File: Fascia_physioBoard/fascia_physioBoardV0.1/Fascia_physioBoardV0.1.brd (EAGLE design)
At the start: 37.3 x 39.1 mm, 88 parts, among them CN2 CA0612KRX7R9BB102, CN3 CA0612KRX7R9BB102, CN4 CA0612KRX7R9BB102, CN5 CA0612KRX7R9BB102, CN6 CA0612KRX7R9BB102, J1 MOLEX_52437-2471MOLEX_52437-2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, J2 MOLEX_52437-2471MOLEX_52437-2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, J3 MOLEX_51296-1294MOLEX_51296-1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, U1 ADS1299-X, U10 TPD4E1B06DCKR, U11 TPD4E1B06DCKR, U12 OPA320AIDBVRDBV5-L, U13 ADUM5028, U2 OPA2320AIDGKT_NOVA8-SOIC-L, U3 OPA2320AIDGKT_NOVAL8-SOIC-L, U4 HCNR200-300E, U5 OPA320AIDBVRDBV5-L, U6 TPD4E1B06DCKR, U7 TPD4E1B06DCKR, U8 TPD4E1B06DCKR, U9 TPD4E1B06DCKR

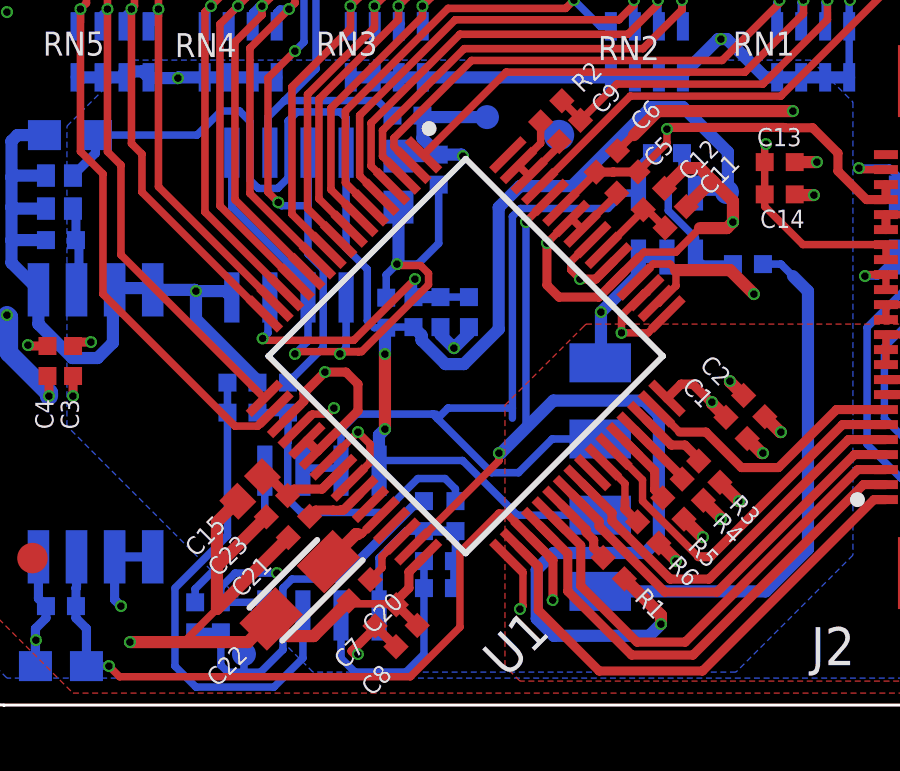
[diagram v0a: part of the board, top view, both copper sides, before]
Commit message: changes to issue with R13
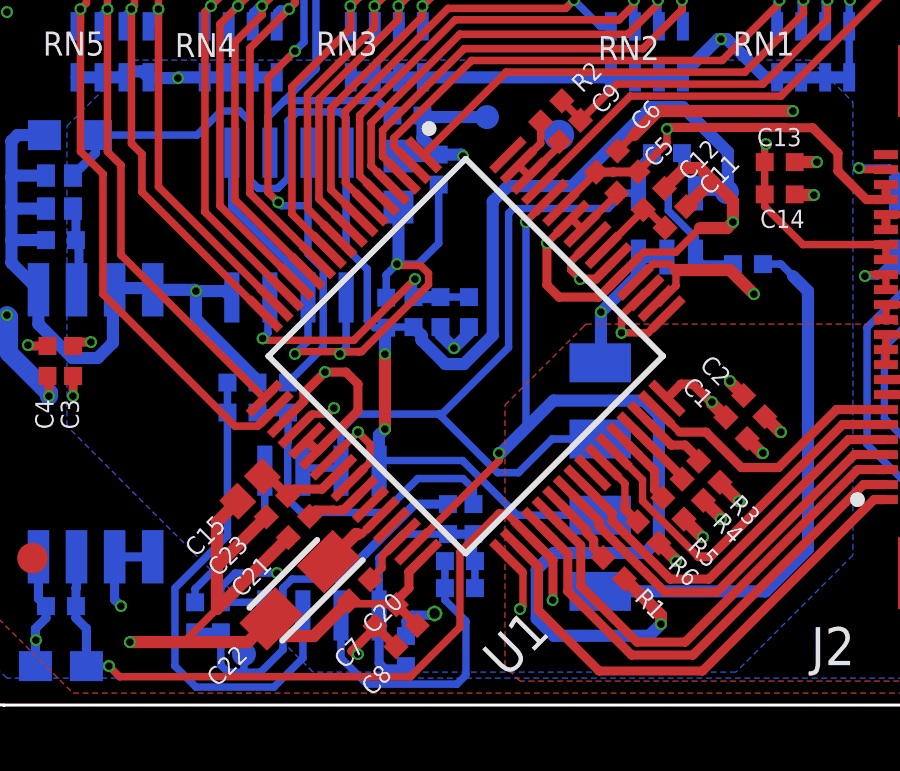
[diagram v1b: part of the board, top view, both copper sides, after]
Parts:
- added R13: 10K, novaXR:0402-TIGHT
- moved R14 0.81 mm to (18.5, 7.40)
- moved C29 0.70 mm to (18.9, 6.00)
- moved R12 0.70 mm to (18.9, 5.10)
- moved C30 0.61 mm to (19.4, 7.40)
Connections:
- net GND_ISO: now also R13.2
- net N$11: now also R13.1
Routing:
- net N$11: track 6.75 -> 9.87 mm
- net N$10: track 7.73 -> 10.2 mm
- net N$15: track 28.3 -> 26.6 mm
- net GND_ISO: track 41.3 -> 42.8 mm, vias 5 -> 6
- net N$4: track 13.0 -> 13.8 mm
- net N$1: track 10.7 -> 11.4 mm

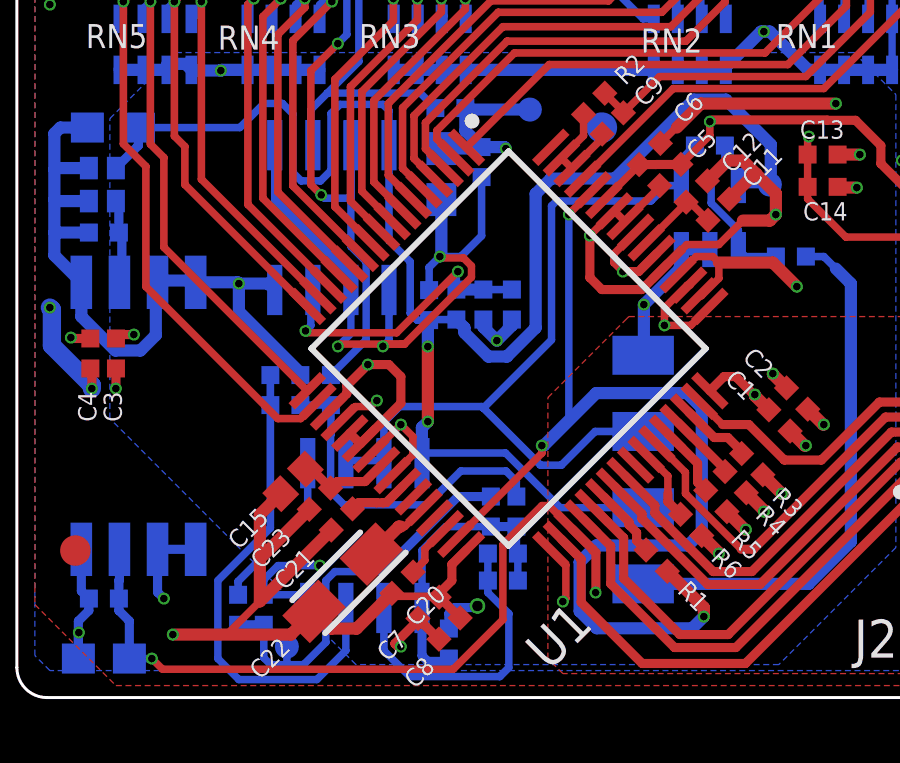
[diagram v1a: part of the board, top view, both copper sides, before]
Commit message: made changes to eda schematic and board files. fixing the issues preventing the V0 to work correctly
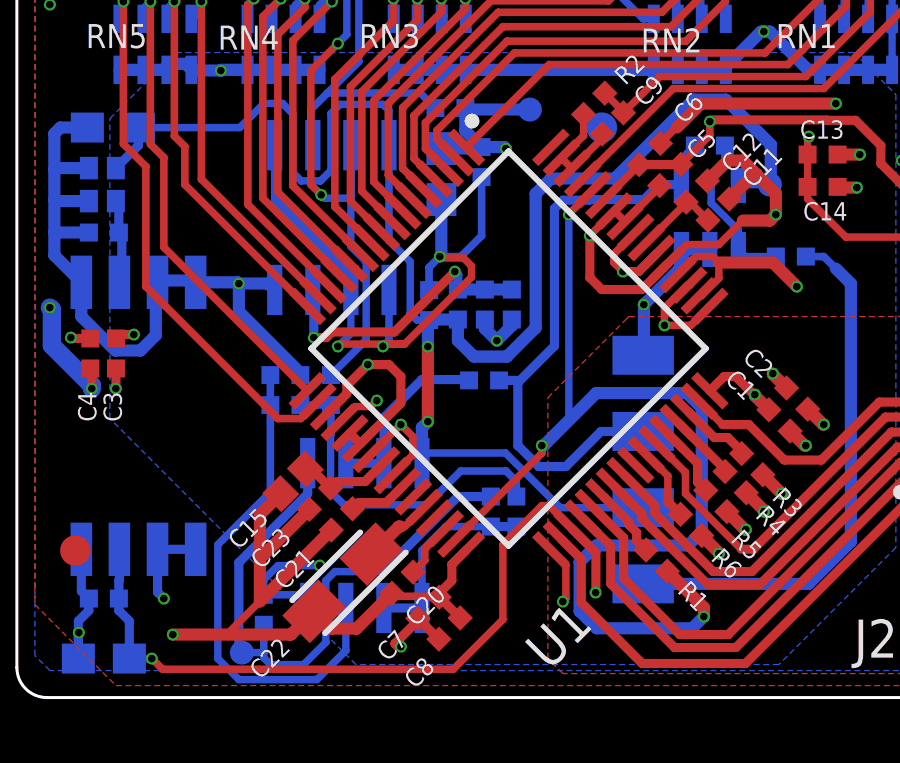
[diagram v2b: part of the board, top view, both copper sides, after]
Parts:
- removed C29: 1nF, novaXR:0402-TIGHT
- removed R12, R13: 10K, novaXR:0402-TIGHT
- removed R8: 140K, novaXR:0402-TIGHT
- added R18: 110K, novaXR:0402-TIGHT
- R7: value 20K -> 10K
- moved R15 11.2 mm to (18.3, 11.8), turned to 180 degrees
- moved RAW_EDA_SIG 1.51 mm to (10.2, 2.70)
- moved R7 0.05 mm to (18.3, 14.3), turned to 90 degrees
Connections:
- removed net N$14: R15.2, U3.5
- removed net N$15: C10.1, U12.4, U3.6, U3.7, U4.3
- new net N$12: C26.1, R18.1, R7.2, U2.3
- net DVDD_ISO: now also R18.2; no longer R8.1
- net GND_ISO: now also R7.1; no longer R13.2, R7.2
- net N$10: now also R15.1, U3.6, U3.7; no longer C29.1, R12.1, U3.2
- net N$11: now also U3.2; no longer C29.2, R12.2, R13.1
- net N$2: now also C10.1, R15.2, U12.4, U4.3; no longer C26.1, R7.1, R8.2, U2.3
- net N$4: now also U3.5; no longer R15.1
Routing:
- net N$15: track 26.6 -> 0.00 mm
- net N$2: track 9.92 -> 20.1 mm, vias 2 -> 0
- net N$12: track 0.00 -> 9.65 mm, vias 0 -> 2
- net N$4: track 13.8 -> 20.3 mm
- net N$14: track 5.35 -> 0.00 mm
- net N$10: track 10.2 -> 6.17 mm
- net N$11: track 9.87 -> 6.66 mm
- net GND_ISO: track 42.8 -> 41.3 mm, vias 6 -> 5

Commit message: Update Fascia_physioBoardV0.1.brd
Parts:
- moved FD3 16.1 mm to (19.0, 4.40)
- moved R16 0.30 mm to (28.8, 15.9)
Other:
- board text added: "FACIA_PHYSIO_V0.1_03/08/20"
- board text removed: "FACIA_PHYSIO_V0.1_03/03/20"
